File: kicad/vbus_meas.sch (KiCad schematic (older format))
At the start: 32 parts, among them U1601 AMC1311B, U1602 AMC1311B, U1603 RFM-0505S, U1604 RFM-0505S

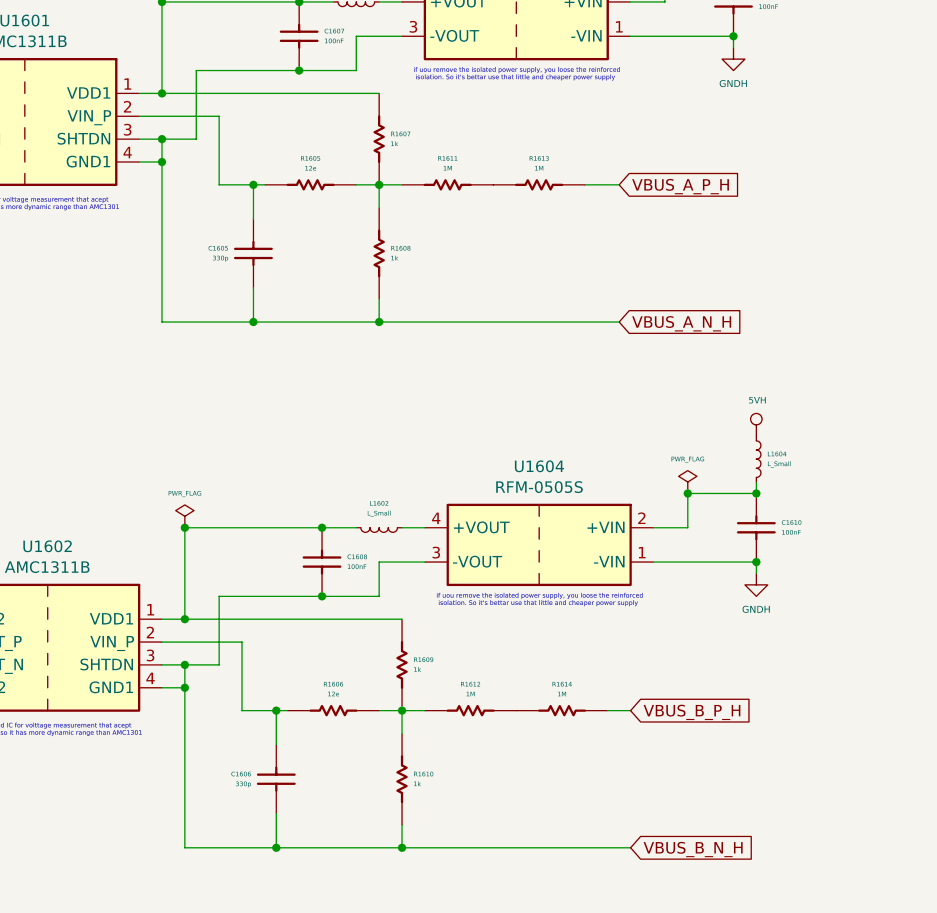
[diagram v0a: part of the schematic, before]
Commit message: All IC placed inside board size but....
I've placed all stuff on board size even thought all are in groups I've
to move the IC to route them. Let's begin
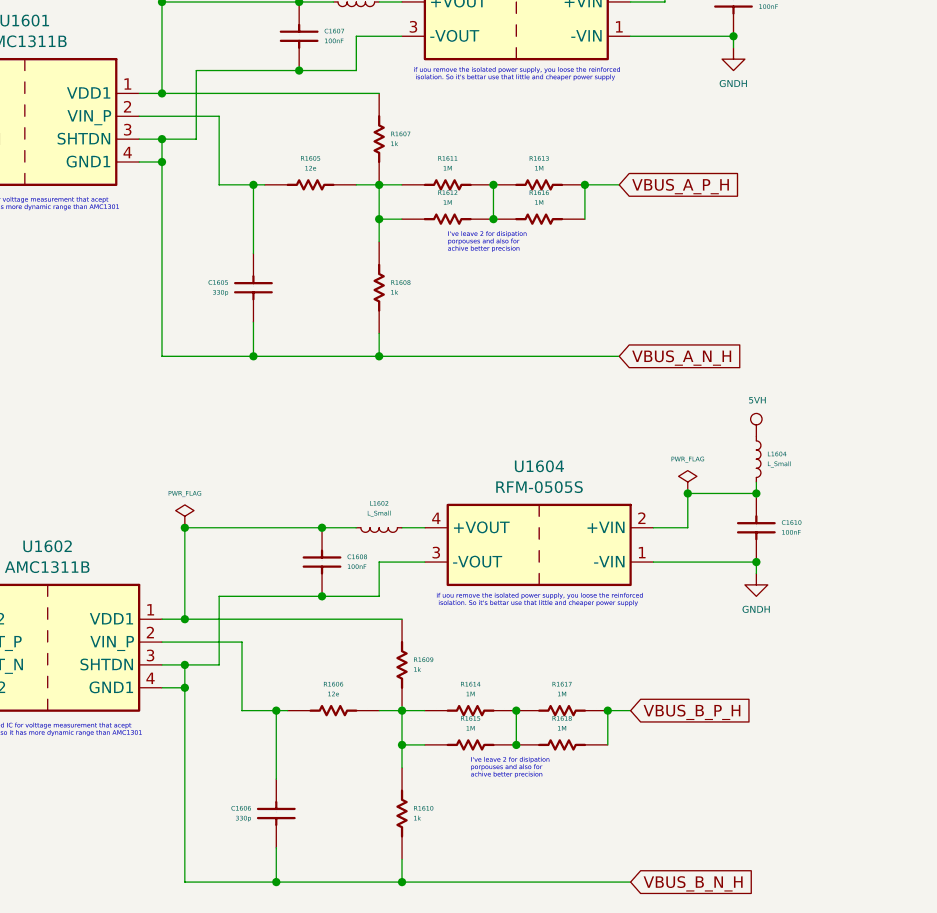
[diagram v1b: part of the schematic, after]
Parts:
- added R1615, R1616, R1617, R1618: 1M, Resistor_SMD:R_1206_3216Metric_Pad1.42x1.75mm_HandSolder, symbol servo:Resistor
- L1601, L1602, L1603, L1604: footprint Inductor_SMD:L_0603_1608Metric -> Inductor_SMD:L_1206_3216Metric_Pad1.42x1.75mm_HandSolder
- R1611, R1612, R1613, R1614: footprint Resistor_SMD:R_0603_1608Metric -> Resistor_SMD:R_1206_3216Metric_Pad1.42x1.75mm_HandSolder
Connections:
- net VBUS_A_P_H: now also R1616.2
- net VBUS_B_P_H: now also R1617.2, R1618.2; no longer R1614.2
- net at R1605.2, R1607.2, R1608.1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: now also R1612.1
- net at R1611.2, R1613.1: now also R1612.2, R1616.1
- net at R1606.2, R1609.2, R1610.1: now also R1614.1, R1615.1; no longer R1612.1
- new net: R1614.2, R1615.2, R1617.1, R1618.1
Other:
- note added: "I've leave 2 for disipation \nporpouses and also for \nachive better precision"
- moved on the sheet: C1605, C1606, R1608, R1610

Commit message: beginine routing... far far away
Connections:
- net VBUS_A_N renamed VBUS1_N
- net VBUS_A_N_H renamed VBUS1_N_H
- net VBUS_A_P renamed VBUS1_P
- net VBUS_A_P_H renamed VBUS1_P_H
- net VBUS_B_N renamed VBUS2_N
- net VBUS_B_N_H renamed VBUS2_N_H
- net VBUS_B_P renamed VBUS2_P
- net VBUS_B_P_H renamed VBUS2_P_H
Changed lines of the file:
@@
 $EndDescr
 Text GLabel 5400 2850 0    50   Input ~ 0
-VBUS_A_P
+VBUS1_P
 Text GLabel 5400 3250 0    50   Input ~ 0
-VBUS_A_N
+VBUS1_N
 Text Notes 4700 1100 0    197  ~ 39
 VBUS -> R divider -> ISO ADC -> uC\n
@@
 It's an isolated specialized IC for volttage measurement that acept\n unipolar signal until 2V, so it has more dynamic range than AMC1301\n for example
 Text GLabel 5500 5150 0    50   Input ~ 0
-VBUS_B_P
+VBUS2_P
 Text GLabel 5500 5550 0    50   Input ~ 0
-VBUS_B_N
+VBUS2_N
 Text Notes 6850 1750 0    39   ~ 0
 It's intended to measure the Vbus, one per motor, but they cold be\n joined if both motor share same VBus. The Vbus informatio will be\n used by the control algorith and to drive the break resistor PWM to\n protect the rise of the Vbus more than a threshold\n\nThe input is expected not to be 220v or 380v. It's supoused to be a\n isolated low voltage to maintaint the reinforced insulation. In case\n you can't you could input 220v directly but the isolation would be\n simple
@@
 Connection ~ 8800 4050
 Text GLabel 9900 6350 2    50   Input ~ 0
-VBUS_B_N_H
+VBUS2_N_H
 Text GLabel 9850 4050 2    50   Input ~ 0
-VBUS_A_N_H
+VBUS1_N_H
 Text GLabel 9900 5600 2    50   Input ~ 0
-VBUS_B_P_H
+VBUS2_P_H
 Text GLabel 9850 3300 2    50   Input ~ 0
-VBUS_A_P_H
+VBUS1_P_H
 Wire Wire Line
 	8900 6350 9900 6350

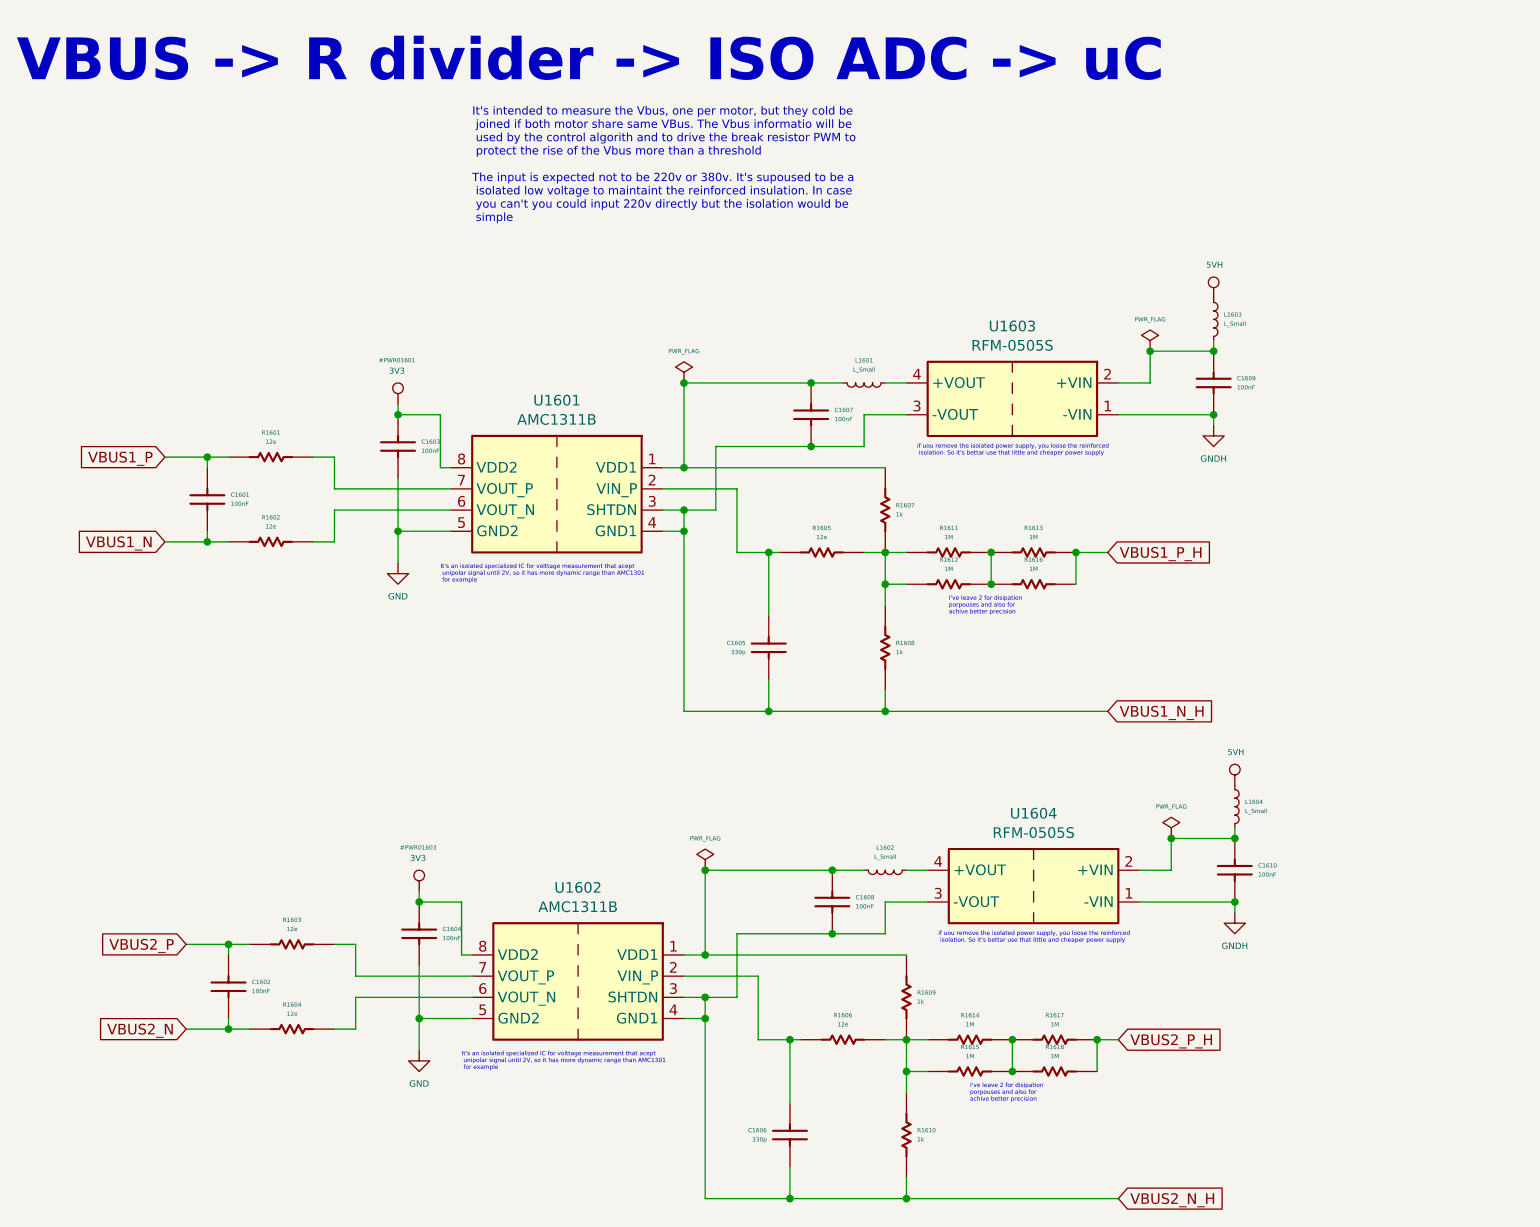
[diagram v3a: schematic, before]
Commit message: added sloted holes everyware
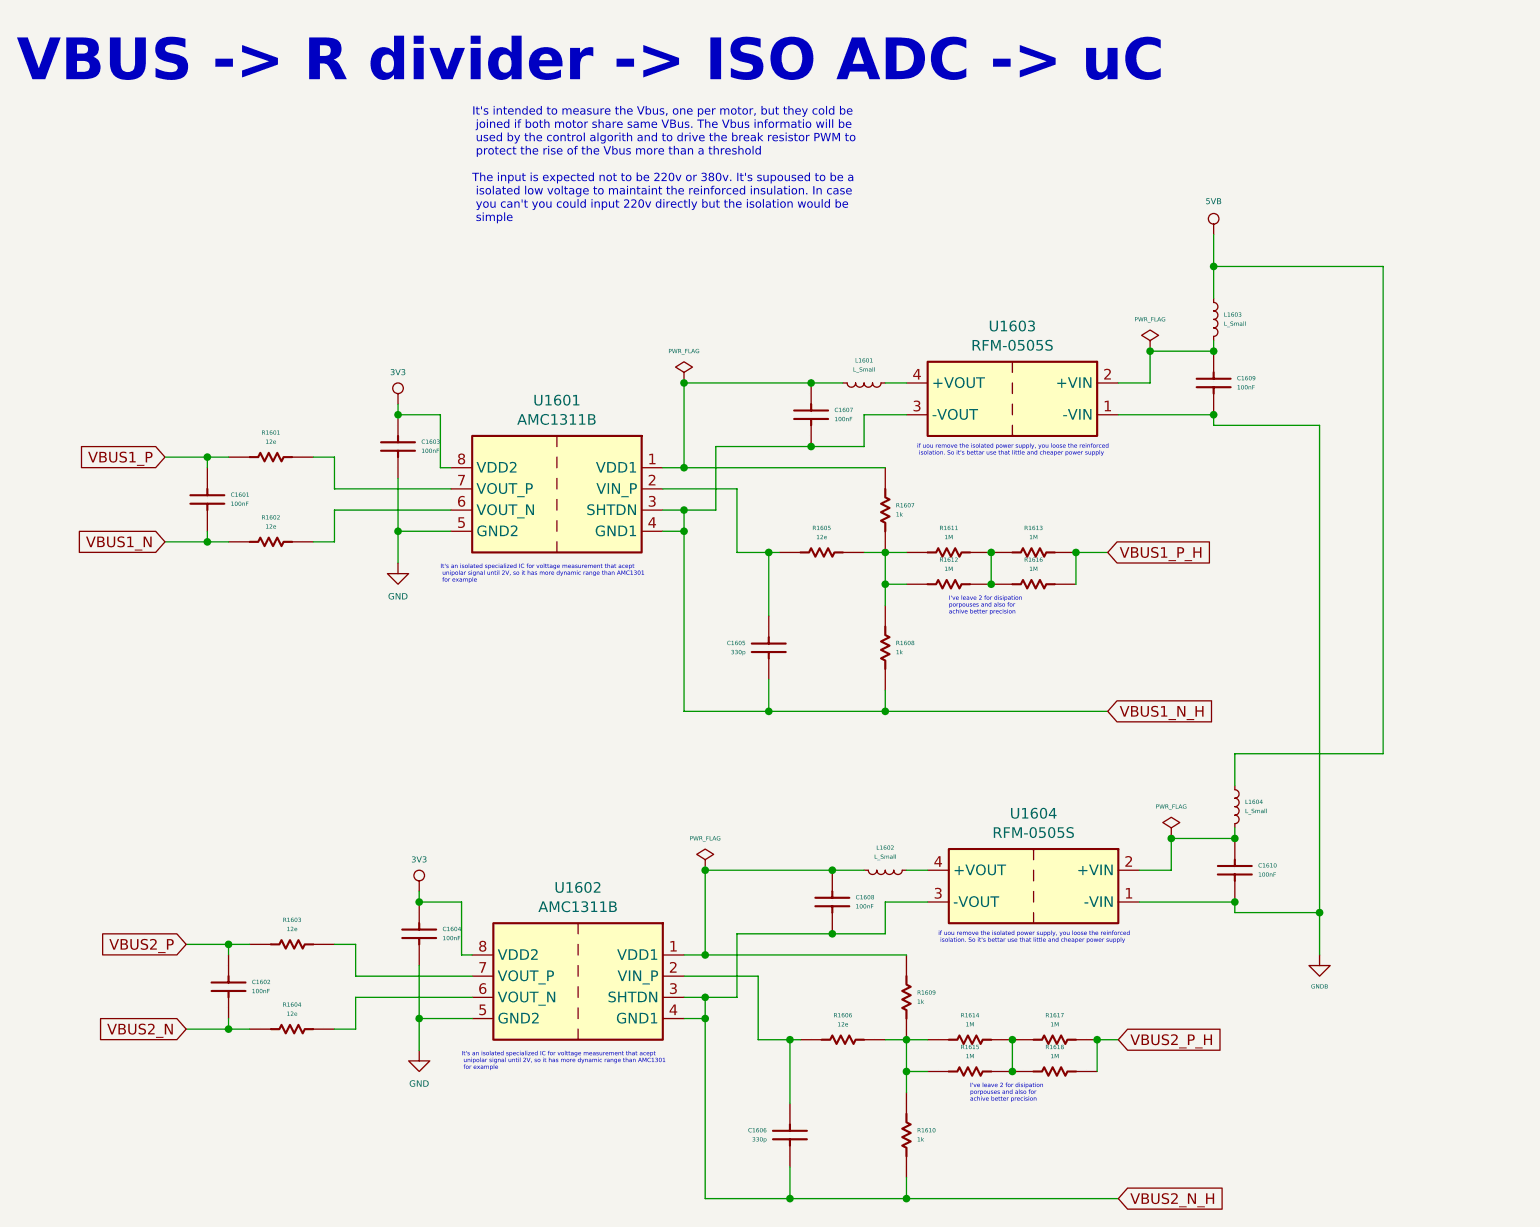
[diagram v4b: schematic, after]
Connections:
- net 5VH renamed 5VB
- net GNDH renamed GNDB
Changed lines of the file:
@@
 AR Path="/605BEC04/5E1AD387" Ref="#PWR01601"  Part="1"
 AR Path="/5DE49152/5E1AD387" Ref="#PWR?"  Part="1"
-F 0 "#PWR01601" H 6505 2807 20  0000 C CNN
-F 1 "3V3" H 6505 2757 28  0000 C CNN
+F 0 "#PWR01601" H 6400 2700 20  0001 C CNN
+F 1 "3V3" H 6500 2750 28  0000 C CNN
 F 2 "" H 6500 2600 50  0001 C CNN
 F 3 "" H 6500 2600 50  0001 C CNN
 	1    6500 2600
-	-1   0    0    -1
+	1    0    0    -1
 $EndComp
 $Comp
@@
 	6500 3200 6500 3350
 Connection ~ 6500 3200
-$Comp
-L servo:5VH #PWR?
-U 1 1 5E1AD3D2
-P 10350 2100
-AR Path="/5DE49152/5E1AD3D2" Ref="#PWR?"  Part="1"
-AR Path="/605BEC04/5E1AD3D2" Ref="#PWR01605"  Part="1"
-F 0 "#PWR01605" H 10350 1900 20  0001 C CNN
-F 1 "5VH" H 10355 2257 28  0000 C CNN
-F 2 "" H 10350 2100 50  0001 C CNN
-F 3 "" H 10350 2100 50  0001 C CNN
-	1    10350 2100
-	1    0    0    -1
-$EndComp
 Wire Wire Line
 	6750 3100 6200 3100
@@
 Wire Wire Line
 	9900 2650 10350 2650
-$Comp
-L servo:GNDH #PWR?
-U 1 1 5E1AD36D
-P 10350 2700
-AR Path="/5DD76B18/5E1AD36D" Ref="#PWR?"  Part="1"
-AR Path="/5DEE980E/5E1AD36D" Ref="#PWR?"  Part="1"
-AR Path="/5E2F3BE3/5E1AD36D" Ref="#PWR?"  Part="1"
-AR Path="/605BEC04/5E1AD36D" Ref="#PWR01606"  Part="1"
-AR Path="/5DE49152/5E1AD36D" Ref="#PWR?"  Part="1"
-F 0 "#PWR01606" H 10350 2450 30  0001 C CNN
-F 1 "GNDH" H 10350 2542 30  0000 C CNN
-F 2 "" H 10350 2700 50  0001 C CNN
-F 3 "" H 10350 2700 50  0001 C CNN
-	1    10350 2700
-	-1   0    0    -1
-$EndComp
 Connection ~ 10350 2650
 $Comp
@@
 AR Path="/605BEC04/5E1B9A70" Ref="#PWR01603"  Part="1"
 AR Path="/5DE49152/5E1B9A70" Ref="#PWR?"  Part="1"
-F 0 "#PWR01603" H 6605 5107 20  0000 C CNN
-F 1 "3V3" H 6605 5057 28  0000 C CNN
+F 0 "#PWR01603" H 6500 5000 20  0001 C CNN
+F 1 "3V3" H 6600 5050 28  0000 C CNN
 F 2 "" H 6600 4900 50  0001 C CNN
 F 3 "" H 6600 4900 50  0001 C CNN
 	1    6600 4900
-	-1   0    0    -1
+	1    0    0    -1
 $EndComp
 $Comp
@@
 	6600 5500 6600 5650
 Connection ~ 6600 5500
-$Comp
-L servo:5VH #PWR?
-U 1 1 5E1B9A98
-P 10450 4400
-AR Path="/5DE49152/5E1B9A98" Ref="#PWR?"  Part="1"
-AR Path="/605BEC04/5E1B9A98" Ref="#PWR01607"  Part="1"
-F 0 "#PWR01607" H 10450 4200 20  0001 C CNN
-F 1 "5VH" H 10455 4557 28  0000 C CNN
-F 2 "" H 10450 4400 50  0001 C CNN
-F 3 "" H 10450 4400 50  0001 C CNN
-	1    10450 4400
-	1    0    0    -1
-$EndComp
 Wire Wire Line
 	6850 5400 6300 5400
@@
 Wire Wire Line
 	10000 4950 10450 4950
-$Comp
-L servo:GNDH #PWR?
-U 1 1 5E1B9B06
-P 10450 5000
-AR Path="/5DD76B18/5E1B9B06" Ref="#PWR?"  Part="1"
-AR Path="/5DEE980E/5E1B9B06" Ref="#PWR?"  Part="1"
-AR Path="/5E2F3BE3/5E1B9B06" Ref="#PWR?"  Part="1"
-AR Path="/605BEC04/5E1B9B06" Ref="#PWR01608"  Part="1"
-AR Path="/5DE49152/5E1B9B06" Ref="#PWR?"  Part="1"
-F 0 "#PWR01608" H 10450 4750 30  0001 C CNN
-F 1 "GNDH" H 10450 4842 30  0000 C CNN
-F 2 "" H 10450 5000 50  0001 C CNN
-F 3 "" H 10450 5000 50  0001 C CNN
-	1    10450 5000
-	-1   0    0    -1
-$EndComp
 Connection ~ 10450 4950
 $Comp
@@
 Connection ~ 9300 3450
 Connection ~ 9300 3300
+$Comp
+L servo:5VB #PWR0158
+U 1 1 5E3C1E64
+P 10350 1800
+F 0 "#PWR0158" H 10350 1600 20  0001 C CNN
+F 1 "5VB" H 10350 1957 28  0000 C CNN
+F 2 "" H 10350 1800 50  0001 C CNN
+F 3 "" H 10350 1800 50  0001 C CNN
+	1    10350 1800
+	1    0    0    -1
+$EndComp
+Wire Wire Line
+	10350 2100 10350 1950
+Wire Wire Line
+	10450 4400 10450 4250
+Wire Wire Line
+	10450 4250 11150 4250
+Wire Wire Line
+	11150 4250 11150 1950
+Wire Wire Line
+	11150 1950 10350 1950
+Connection ~ 10350 1950
+Wire Wire Line
+	10350 1950 10350 1800
+$Comp
+L servo:GNDB #PWR0159
+U 1 1 5E3D9428
+P 10850 5200
+F 0 "#PWR0159" H 10850 4950 30  0001 C CNN
+F 1 "GNDB" H 10850 5051 20  0000 C CNN
+F 2 "" H 10850 5200 50  0001 C CNN
+F 3 "" H 10850 5200 50  0001 C CNN
+	1    10850 5200
+	1    0    0    -1
+$EndComp
+Wire Wire Line
+	10450 5000 10850 5000
+Wire Wire Line
+	10850 5000 10850 5200
+Wire Wire Line
+	10850 5000 10850 2700
+Wire Wire Line
+	10850 2700 10350 2700
+Connection ~ 10850 5000
 $EndSCHEMATC
